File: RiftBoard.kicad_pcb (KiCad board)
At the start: 2 copper layers, 21 x 51 mm, 38 parts, among them J1 USB_C_Receptacle_USB2.0_14P, J2 Conn_01x20, J3 Conn_01x20, J4 Conn_01x03, SW1 SW_Push, SW2 SW_Push, U1 RP2040, U2 MCP1700x-330xxTT, U3 W25Q16JVUXIQ TR, Y1 12MHz

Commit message: 10:19 logoff
Decoupling caps, and differential data line done
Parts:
- moved C22 41.4 mm to (101.0, 79.1), turned to 180 degrees
- moved C7 35.2 mm to (108.2, 95.8)
- moved R4 35.1 mm to (104.9, 94.8), turned to -90 degrees
- moved R3 33.6 mm to (106.0, 94.8), turned to -90 degrees
- moved C2 32.5 mm to (109.0, 97.2), turned to -90 degrees
- moved C1 32.4 mm to (108.5, 94.7)
- moved C9 31.7 mm to (107.0, 93.2), turned to 90 degrees
- moved C3 30.4 mm to (110.4, 97.7)
- moved C8 26.2 mm to (108.0, 93.2), turned to 90 degrees
- moved C6 26.0 mm to (110.4, 96.7)
- moved C5 21.5 mm to (109.0, 93.2), turned to 90 degrees
- moved C4 20.2 mm to (110.0, 95.2), turned to -90 degrees
- moved C26 20.1 mm to (100.2, 86.8)
- moved U2 2.40 mm to (101.8, 81.8), turned to 90 degrees
- moved C11 2.31 mm to (108.0, 91.8), turned to 0 degrees
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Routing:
- net USB_D-: track 0.00 -> 17.9 mm
- net USB_D+: track 0.00 -> 17.8 mm
- net +3V3: track 4.86 -> 14.6 mm
- net GND: track 11.3 -> 6.59 mm
- net Net-(C25-Pad2): track 1.60 -> 5.78 mm
- net +1V1: track 5.15 -> 8.93 mm, vias 0 -> 2
- net Net-(U1-USB_DP): track 0.00 -> 1.57 mm
- net Net-(U1-USB_DM): track 0.00 -> 1.45 mm

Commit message: Pre-routing
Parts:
- moved SW1 58.9 mm to (100.3, 114.9)
- moved SW2 50.4 mm to (108.2, 114.9)
- moved R2 47.4 mm to (103.0, 79.3), turned to -90 degrees
- moved R6 44.1 mm to (99.8, 90.8), turned to -90 degrees
- moved C23 39.7 mm to (101.7, 85.2), turned to 180 degrees
- moved R1 36.3 mm to (105.6, 79.2), turned to -90 degrees
- moved R7 35.3 mm to (100.3, 111.2), turned to 180 degrees
- moved D1 33.9 mm to (108.0, 111.4)
- moved D2 32.2 mm to (108.0, 107.3)
- moved R8 30.0 mm to (108.0, 106.0)
- moved R9 29.1 mm to (108.0, 110.1)
- moved C26 5.06 mm to (103.0, 91.0), turned to 90 degrees
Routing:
- net +3V3: track 14.6 -> 19.6 mm
- net Net-(U2-VO): track 0.00 -> 2.54 mm
- net QSPI_SS: track 9.54 -> 10.7 mm

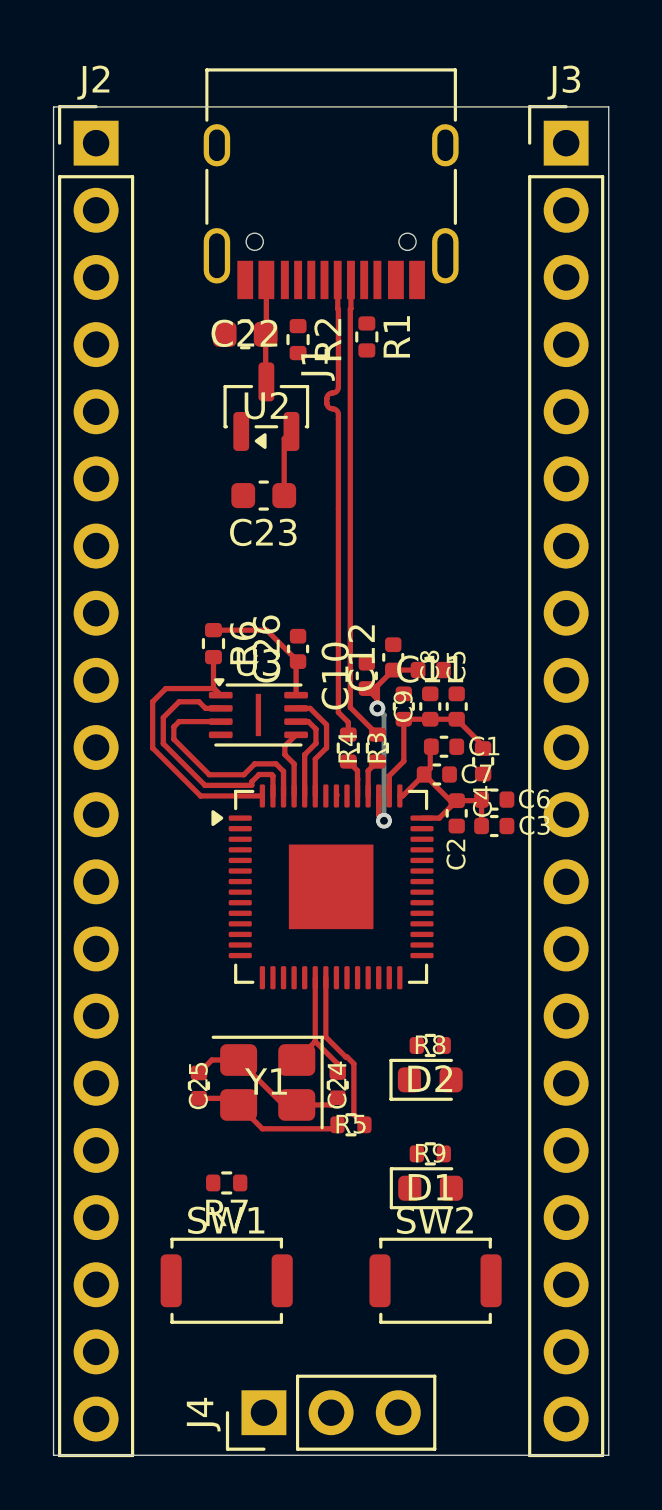
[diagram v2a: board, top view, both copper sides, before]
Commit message: Failed to trace without swapping gpio around, Im going to flip pin header for better compatibility with rp2040.
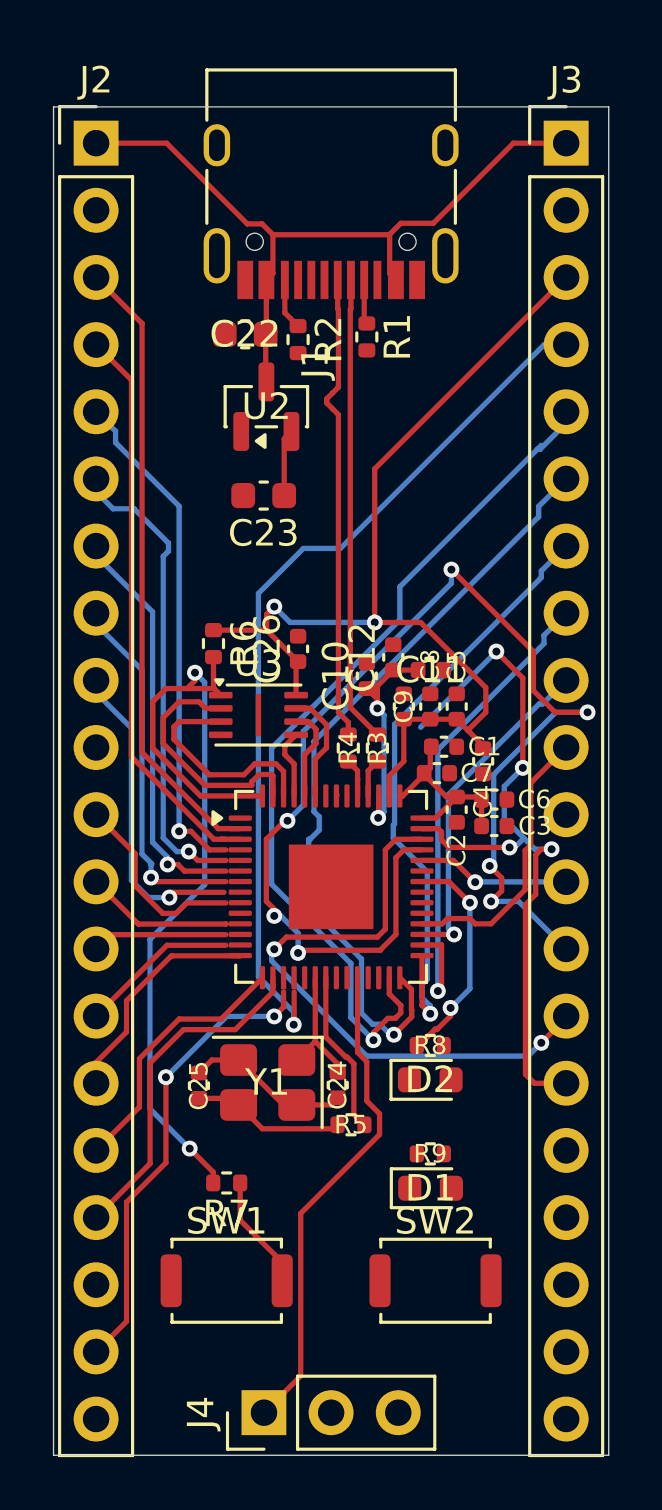
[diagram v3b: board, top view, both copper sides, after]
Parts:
- moved C2 0.14 mm to (109.0, 97.1)
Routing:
- net GPIO27/ADC1: track 0.00 -> 48.5 mm, vias 0 -> 7
- net GPIO16: track 0.00 -> 33.9 mm, vias 0 -> 1
- net GPIO15: track 0.00 -> 33.7 mm, vias 0 -> 1
- net GPIO17: track 0.00 -> 29.9 mm, vias 0 -> 1
- net GPIO29/ADC3: track 0.00 -> 28.6 mm, vias 0 -> 4
- net +3V3: track 19.6 -> 48.0 mm, vias 0 -> 2
- net VBUS: track 3.88 -> 28.2 mm
- net GPIO18: track 0.00 -> 23.7 mm, vias 0 -> 1
- net GPIO0: track 0.00 -> 23.6 mm
- net GPIO28/ADC2: track 0.00 -> 22.8 mm, vias 0 -> 2
- net QSPI_SS: track 10.7 -> 32.8 mm, vias 0 -> 2
- net GPIO1: track 0.00 -> 21.7 mm
- net GPIO2: track 0.00 -> 19.7 mm, vias 0 -> 1
- net GPIO19: track 0.00 -> 19.1 mm, vias 0 -> 1
- net SWCLK: track 0.00 -> 18.6 mm
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
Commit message: Finished PCB stuffs, now just design and I can move on to the production and assembly.
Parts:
- added G***: LOGO, RiftBoard:rift-portal, B.Cu at (104.2, 107.8)
- moved C1 0.79 mm to (107.7, 94.7)
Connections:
- J3 pad 10: GPIO21 -> GPIO23
- J3 pad 12: GPIO26/ADC0 -> GPIO22
- J3 pad 13: GPIO27/ADC1 -> GPIO21
- J3 pad 14: GPIO28/ADC2 -> GPIO20
- J3 pad 15: GPIO29/ADC3 -> GPIO19
- J3 pad 17: GPIO22 -> GPIO18
- J3 pad 4: GPIO15 -> GPIO29/ADC3
- J3 pad 5: GPIO16 -> GPIO28/ADC2
- J3 pad 6: GPIO17 -> GPIO27/ADC1
- J3 pad 7: GPIO18 -> GPIO26/ADC0
- J3 pad 8: GPIO19 -> GPIO25
- J3 pad 9: GPIO20 -> GPIO24
- R8 pad 1: Net-(U1-GPIO24) -> Net-(U1-GPIO15)
- R9 pad 1: Net-(U1-GPIO25) -> Net-(U1-GPIO16)
- SW2 pad 1: GPIO23 -> GPIO17
- U1 pad 18: GPIO15 -> Net-(U1-GPIO15)
- U1 pad 27: GPIO16 -> Net-(U1-GPIO16)
- U1 pad 36: Net-(U1-GPIO24) -> GPIO24
- U1 pad 37: Net-(U1-GPIO25) -> GPIO25
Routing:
- net GND: track 6.59 -> 141.6 mm, vias 0 -> 19
- net +3V3: track 48.0 -> 94.8 mm, vias 2 -> 7
- net GPIO23: track 0.00 -> 38.2 mm, vias 0 -> 4
- net GPIO16: track 33.9 -> 0.00 mm, vias 1 -> 0
- net GPIO15: track 33.7 -> 0.00 mm, vias 1 -> 0
- net GPIO27/ADC1: track 48.5 -> 19.7 mm, vias 7 -> 1
- net GPIO24: track 0.00 -> 26.1 mm, vias 0 -> 2
- net GPIO25: track 0.00 -> 19.4 mm, vias 0 -> 2
- net SWDIO: track 0.00 -> 19.3 mm
- net RUN: track 0.00 -> 16.8 mm, vias 0 -> 1
- net GPIO17: track 29.9 -> 14.3 mm, vias 1 -> 0
- net GPIO26/ADC0: track 6.53 -> 21.1 mm, vias 1 -> 2
- net GPIO19: track 19.1 -> 8.73 mm, vias 1 -> 0
- net GPIO18: track 23.7 -> 13.6 mm, vias 1 -> 0
- net Net-(U1-GPIO24): track 8.47 -> 0.00 mm, vias 2 -> 0
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- added copper zone on B.Cu, net GND
- added copper zone on F.Cu, net GND
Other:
- board size 21 x 51 mm -> 21 x 51.2 mm
- board text added: "RIFTBOARD"

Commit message: submission
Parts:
- added G***: LOGO, RiftBoard:fedcrov, B.Cu at (101.8, 85.9)
- added G***: LOGO, RiftBoard:hackclubflag, B.Cu at (104.2, 75.0)
- J1: value USB_C_Receptacle_USB2.0_14P -> USB_C_Receptacle_USB2.0_16P
- moved J1 0.06 mm to (104.2, 73.0)
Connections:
- J1 pad A8: (no net) -> unconnected-(J1-SBU1-PadA8)
- J1 pad B8: (no net) -> unconnected-(J1-SBU2-PadB8)
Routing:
- net GND: track 141.6 -> 200.0 mm, vias 19 -> 22
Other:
- board text added: "MADE BY CASPIAN"

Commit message: Hopefully final fix
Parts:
- moved C11 14.6 mm to (105.2, 106.1), turned to -90 degrees
- moved C5 13.8 mm to (104.2, 106.1), turned to -90 degrees
- moved C6 13.0 mm to (98.1, 101.0), turned to 180 degrees
- moved C7 8.26 mm to (100.0, 96.1), turned to 90 degrees
- moved C4 5.76 mm to (110.4, 101.0), turned to 0 degrees
- moved C8 4.18 mm to (103.9, 94.0)
- moved C9 3.28 mm to (103.9, 92.1)
- moved C10 3.22 mm to (107.0, 94.9)
- moved C26 2.70 mm to (100.9, 89.3)
- moved C25 2.56 mm to (98.3, 109.9)
- moved C12 2.19 mm to (108.0, 93.0)
- moved R5 2.14 mm to (104.1, 110.9)
- moved R7 2.06 mm to (101.9, 112.5)
- moved C3 1.86 mm to (109.0, 96.5)
- moved R1 1.81 mm to (107.4, 79.4)
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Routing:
- net GPIO23: track 38.2 -> 9.51 mm, vias 4 -> 0
- net +3V3: track 94.8 -> 115.9 mm, vias 7 -> 4
- net GND: track 200.0 -> 217.5 mm, vias 22 -> 17
- net GPIO24: track 26.1 -> 11.6 mm, vias 2 -> 0
- net QSPI_SS: track 31.8 -> 40.8 mm
- net GPIO29/ADC3: track 28.0 -> 21.5 mm, vias 1 -> 0
- net GPIO25: track 19.4 -> 13.6 mm, vias 2 -> 0
- net GPIO26/ADC0: track 21.1 -> 15.8 mm, vias 2 -> 1
- net XOUT: track 6.20 -> 11.4 mm, vias 0 -> 2
- net +1V1: track 12.7 -> 16.8 mm
- net Net-(U1-GPIO15): track 6.50 -> 10.4 mm
- net GPIO17: track 14.3 -> 17.4 mm
- net GPIO28/ADC2: track 21.6 -> 19.4 mm, vias 1 -> 0
- net GPIO27/ADC1: track 19.7 -> 17.7 mm
- net Net-(R7-Pad1): track 4.36 -> 2.40 mm
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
